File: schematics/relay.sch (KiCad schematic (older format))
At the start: 0 parts

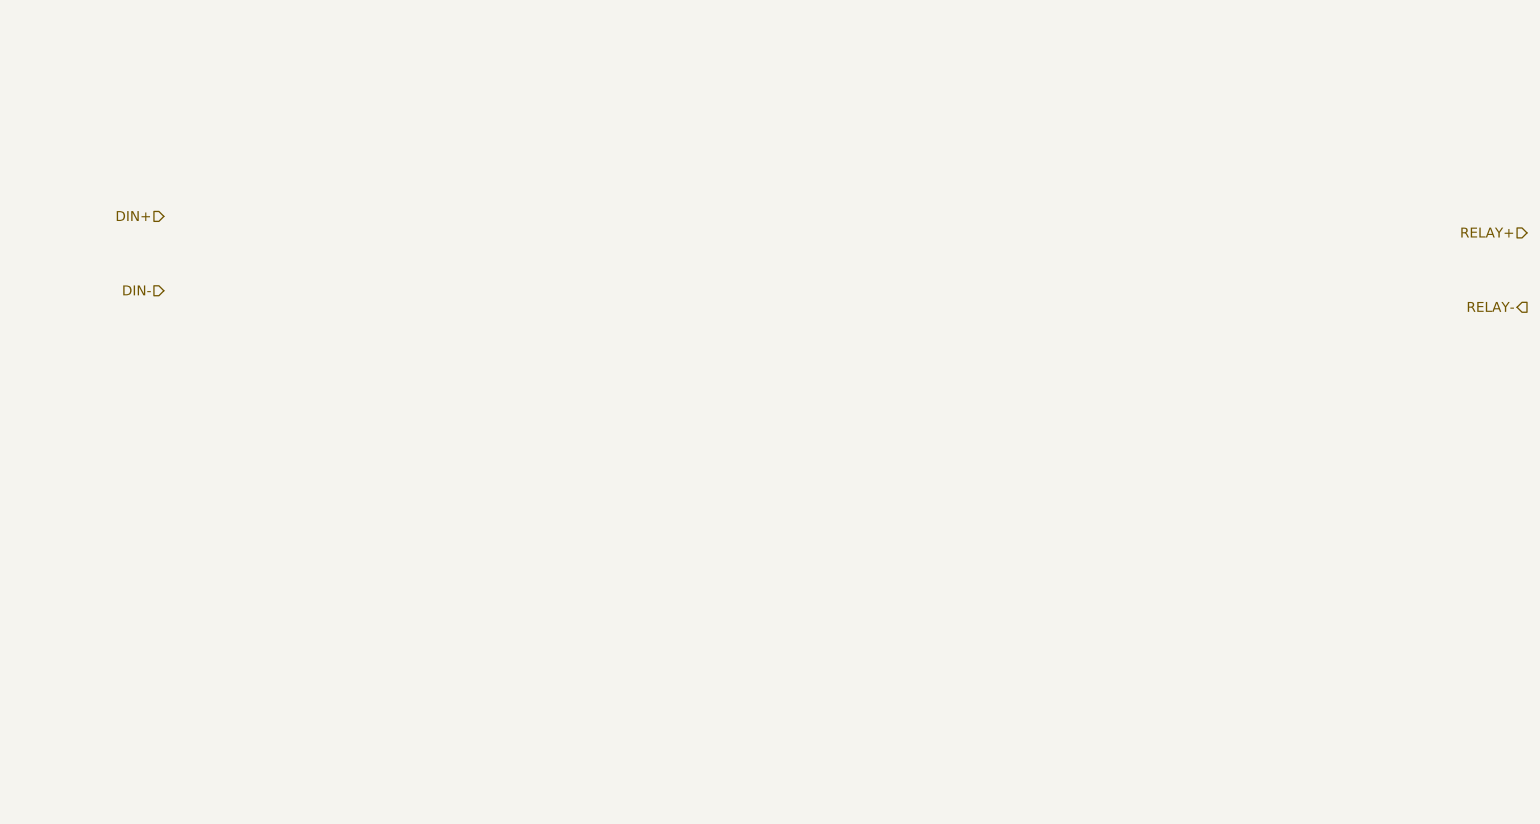
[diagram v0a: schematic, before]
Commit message: started to add to relay sch
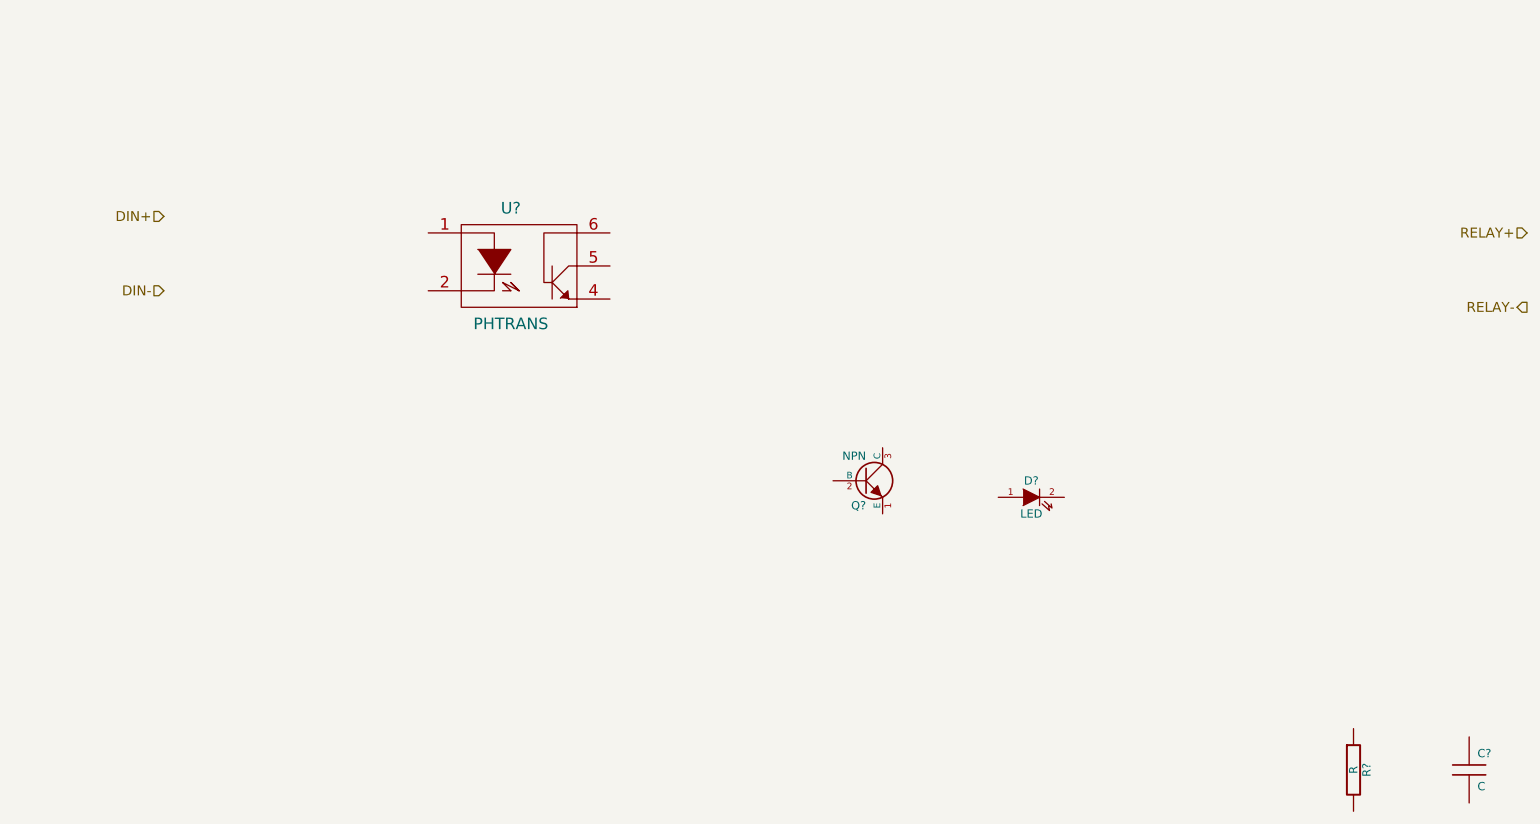
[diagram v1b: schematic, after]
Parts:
- added C?: C, symbol C
- added D?: LED, symbol LED
- added Q?: NPN, symbol NPN
- added R?: R, symbol R
- added U?: PHTRANS, symbol PHTRANS
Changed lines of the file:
@@
-EESchema Schematic File Version 2  date Sat 05 Oct 2013 10:04:00 PM EDT
+EESchema Schematic File Version 2  date Sat 05 Oct 2013 10:37:10 PM EDT
 LIBS:power
 LIBS:device
@@
 LIBS:contrib
 LIBS:valves
+LIBS:relays
 LIBS:benchBuddy-cache
 EELAYER 25  0
@@
 Comment4 ""
 $EndDescr
+$Comp
+L LED D?
+U 1 1 5250C851
+P 6700 4350
+F 0 "D?" H 6700 4450 50  0000 C CNN
+F 1 "LED" H 6700 4250 50  0000 C CNN
+	1    6700 4350
+	1    0    0    -1
+$EndComp
+$Comp
+L NPN Q?
+U 1 1 5250C842
+P 5700 4250
+F 0 "Q?" H 5700 4100 50  0000 R CNN
+F 1 "NPN" H 5700 4400 50  0000 R CNN
+	1    5700 4250
+	1    0    0    -1
+$EndComp
+$Comp
+L PHTRANS U?
+U 1 1 5250C7F3
+P 3600 2950
+F 0 "U?" H 3550 3300 70  0000 C CNN
+F 1 "PHTRANS" H 3550 2600 70  0000 C CNN
+	1    3600 2950
+	1    0    0    -1
+$EndComp
+$Comp
+L R R?
+U 1 1 5250C7C4
+P 8650 6000
+F 0 "R?" V 8730 6000 50  0000 C CNN
+F 1 "R" V 8650 6000 50  0000 C CNN
+	1    8650 6000
+	1    0    0    -1
+$EndComp
+$Comp
+L C C?
+U 1 1 5250C7B7
+P 9350 6000
+F 0 "C?" H 9400 6100 50  0000 L CNN
+F 1 "C" H 9400 5900 50  0000 L CNN
+	1    9350 6000
+	1    0    0    -1
+$EndComp
 Text HLabel 9700 3200 0    60   Output ~ 0
 RELAY-

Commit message: finished block diagram of relay circuitry
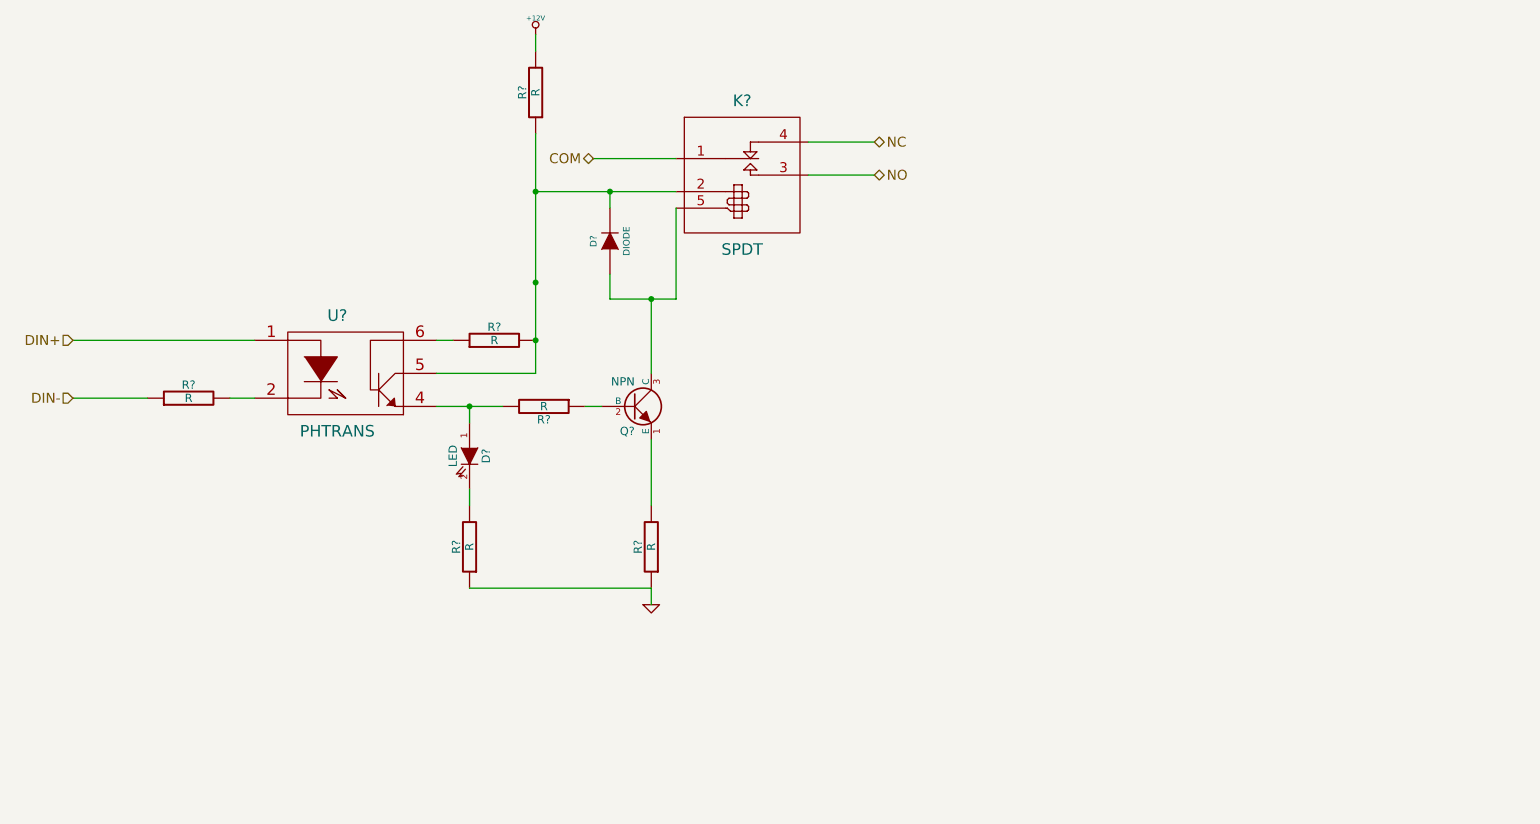
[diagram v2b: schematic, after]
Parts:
- removed C?: C, symbol C
- added D?: DIODE, symbol DIODE
- added K?: SPDT, symbol SPDT
- added R? (x5): R, symbol R
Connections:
- net DIN+: now also U?.1
- net DIN-: now also R?.1
- net at R?.1: now also Q?.2 (B)
- net at R?.2: now also D?.1 (A), U?.4
- net at U?.2: now also R?.2
- net at U?.5: now also D?.2 (K), K?.2 (COIL+), R?.1, R?.2
- net at U?.6: now also R?.1
- net at Q?.1 (E): now also R?.2
- net at Q?.3 (C): now also D?.1 (A), K?.5 (COIL-)
- net at D?.2 (K): now also R?.2
- new net +12V: R?.2
- new net COM: K?.1 (COM)
- new net GND: R?.1, R?.1
- new net NC: K?.4 (NC)
- new net NO: K?.3 (NO)
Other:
- moved on the sheet: D?, Q?, R?, U?
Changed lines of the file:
@@
-EESchema Schematic File Version 2  date Sat 05 Oct 2013 10:37:10 PM EDT
+EESchema Schematic File Version 2  date Sat 05 Oct 2013 10:55:51 PM EDT
 LIBS:power
 LIBS:device
@@
 Comment4 ""
 $EndDescr
+Connection ~ 4150 2500
+Wire Wire Line
+	4150 2600 4150 2500
+Wire Wire Line
+	4150 3000 4150 3150
+Connection ~ 3700 3050
+Wire Wire Line
+	3700 2500 4550 2500
+Wire Wire Line
+	1350 3750 900  3750
+Connection ~ 3700 3400
+Wire Wire Line
+	3200 3400 3100 3400
+Connection ~ 4400 3150
+Wire Wire Line
+	3300 4300 3300 4400
+Wire Wire Line
+	4400 4000 4400 4400
+Wire Wire Line
+	4400 5000 4400 4900
+Wire Wire Line
+	4400 3600 4400 3150
+Wire Wire Line
+	5750 2400 5350 2400
+Wire Wire Line
+	4550 2300 4050 2300
+Wire Wire Line
+	5750 2200 5350 2200
+Wire Wire Line
+	4100 3800 4000 3800
+Wire Wire Line
+	3500 3800 3100 3800
+Wire Wire Line
+	4400 4900 3300 4900
+Wire Wire Line
+	3300 3900 3300 3800
+Connection ~ 3300 3800
+Wire Wire Line
+	3700 1650 3700 1550
+Wire Wire Line
+	3100 3600 3700 3600
+Wire Wire Line
+	1850 3750 2000 3750
+Wire Wire Line
+	2000 3400 900  3400
+Wire Wire Line
+	3700 3600 3700 2150
+Connection ~ 3700 2500
+Wire Wire Line
+	4550 2600 4550 3150
+Wire Wire Line
+	4550 3150 4150 3150
+$Comp
+L DIODE D?
+U 1 1 5250D0C2
+P 4150 2800
+F 0 "D?" H 4150 2900 40  0000 C CNN
+F 1 "DIODE" H 4150 2700 40  0000 C CNN
+	1    4150 2800
+	0    -1   -1   0
+$EndComp
+$Comp
+L R R?
+U 1 1 5250D045
+P 1600 3750
+F 0 "R?" V 1680 3750 50  0000 C CNN
+F 1 "R" V 1600 3750 50  0000 C CNN
+	1    1600 3750
+	0    -1   -1   0
+$EndComp
+$Comp
+L R R?
+U 1 1 5250CFF8
+P 3450 3400
+F 0 "R?" V 3530 3400 50  0000 C CNN
+F 1 "R" V 3450 3400 50  0000 C CNN
+	1    3450 3400
+	0    -1   -1   0
+$EndComp
+$Comp
+L R R?
+U 1 1 5250CFB7
+P 3700 1900
+F 0 "R?" V 3780 1900 50  0000 C CNN
+F 1 "R" V 3700 1900 50  0000 C CNN
+	1    3700 1900
+	-1   0    0    1
+$EndComp
+$Comp
+L +12V #PWR?
+U 1 1 5250CFB1
+P 3700 1550
+F 0 "#PWR?" H 3700 1500 20  0001 C CNN
+F 1 "+12V" H 3700 1650 30  0000 C CNN
+	1    3700 1550
+	1    0    0    -1
+$EndComp
+$Comp
+L R R?
+U 1 1 5250CF99
+P 3300 4650
+F 0 "R?" V 3380 4650 50  0000 C CNN
+F 1 "R" V 3300 4650 50  0000 C CNN
+	1    3300 4650
+	-1   0    0    1
+$EndComp
+$Comp
+L R R?
+U 1 1 5250CEEB
+P 4400 4650
+F 0 "R?" V 4480 4650 50  0000 C CNN
+F 1 "R" V 4400 4650 50  0000 C CNN
+	1    4400 4650
+	-1   0    0    1
+$EndComp
+$Comp
+L GND #PWR?
+U 1 1 5250CEE3
+P 4400 5000
+F 0 "#PWR?" H 4400 5000 30  0001 C CNN
+F 1 "GND" H 4400 4930 30  0001 C CNN
+	1    4400 5000
+	1    0    0    -1
+$EndComp
+Text HLabel 4050 2300 0    60   BiDi ~ 0
+COM
+$Comp
+L SPDT K?
+U 1 1 5250CD3C
+P 4950 2400
+F 0 "K?" H 4950 2850 70  0000 C CNN
+F 1 "SPDT" H 4950 1950 70  0000 C CNN
+	1    4950 2400
+	1    0    0    -1
+$EndComp
 $Comp
 L LED D?
 U 1 1 5250C851
-P 6700 4350
-F 0 "D?" H 6700 4450 50  0000 C CNN
-F 1 "LED" H 6700 4250 50  0000 C CNN
-	1    6700 4350
-	1    0    0    -1
+P 3300 4100
+F 0 "D?" H 3300 4200 50  0000 C CNN
+F 1 "LED" H 3300 4000 50  0000 C CNN
+	1    3300 4100
+	0    1    1    0
 $EndComp
 $Comp
 L NPN Q?
 U 1 1 5250C842
-P 5700 4250
-F 0 "Q?" H 5700 4100 50  0000 R CNN
-F 1 "NPN" H 5700 4400 50  0000 R CNN
-	1    5700 4250
+P 4300 3800
+F 0 "Q?" H 4300 3650 50  0000 R CNN
+F 1 "NPN" H 4300 3950 50  0000 R CNN
+	1    4300 3800
 	1    0    0    -1
 $EndComp
@@
 L PHTRANS U?
 U 1 1 5250C7F3
-P 3600 2950
-F 0 "U?" H 3550 3300 70  0000 C CNN
-F 1 "PHTRANS" H 3550 2600 70  0000 C CNN
-	1    3600 2950
+P 2550 3600
+F 0 "U?" H 2500 3950 70  0000 C CNN
+F 1 "PHTRANS" H 2500 3250 70  0000 C CNN
+	1    2550 3600
 	1    0    0    -1
 $EndComp
@@
 L R R?
 U 1 1 5250C7C4
-P 8650 6000
-F 0 "R?" V 8730 6000 50  0000 C CNN
-F 1 "R" V 8650 6000 50  0000 C CNN
-	1    8650 6000
-	1    0    0    -1
-$EndComp
-$Comp
-L C C?
-U 1 1 5250C7B7
-P 9350 6000
-F 0 "C?" H 9400 6100 50  0000 L CNN
-F 1 "C" H 9400 5900 50  0000 L CNN
-	1    9350 6000
-	1    0    0    -1
-$EndComp
-Text HLabel 9700 3200 0    60   Output ~ 0
-RELAY-
-Text HLabel 9700 2750 0    60   Input ~ 0
-RELAY+
-Text HLabel 1450 3100 0    60   Input ~ 0
+P 3750 3800
+F 0 "R?" V 3830 3800 50  0000 C CNN
+F 1 "R" V 3750 3800 50  0000 C CNN
+	1    3750 3800
+	0    1    1    0
+$EndComp
+Text HLabel 5750 2400 2    60   BiDi ~ 0
+NO
+Text HLabel 5750 2200 2    60   BiDi ~ 0
+NC
+Text HLabel 900  3750 0    60   Input ~ 0
 DIN-
-Text HLabel 1450 2650 0    60   Input ~ 0
+Text HLabel 900  3400 0    60   Input ~ 0
 DIN+
 $EndSCHEMATC
